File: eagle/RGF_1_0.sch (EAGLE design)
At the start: 14 parts, among them IC1 74HC670N, X1 IN, X2 Addr, X3 MODE, X4 OUT

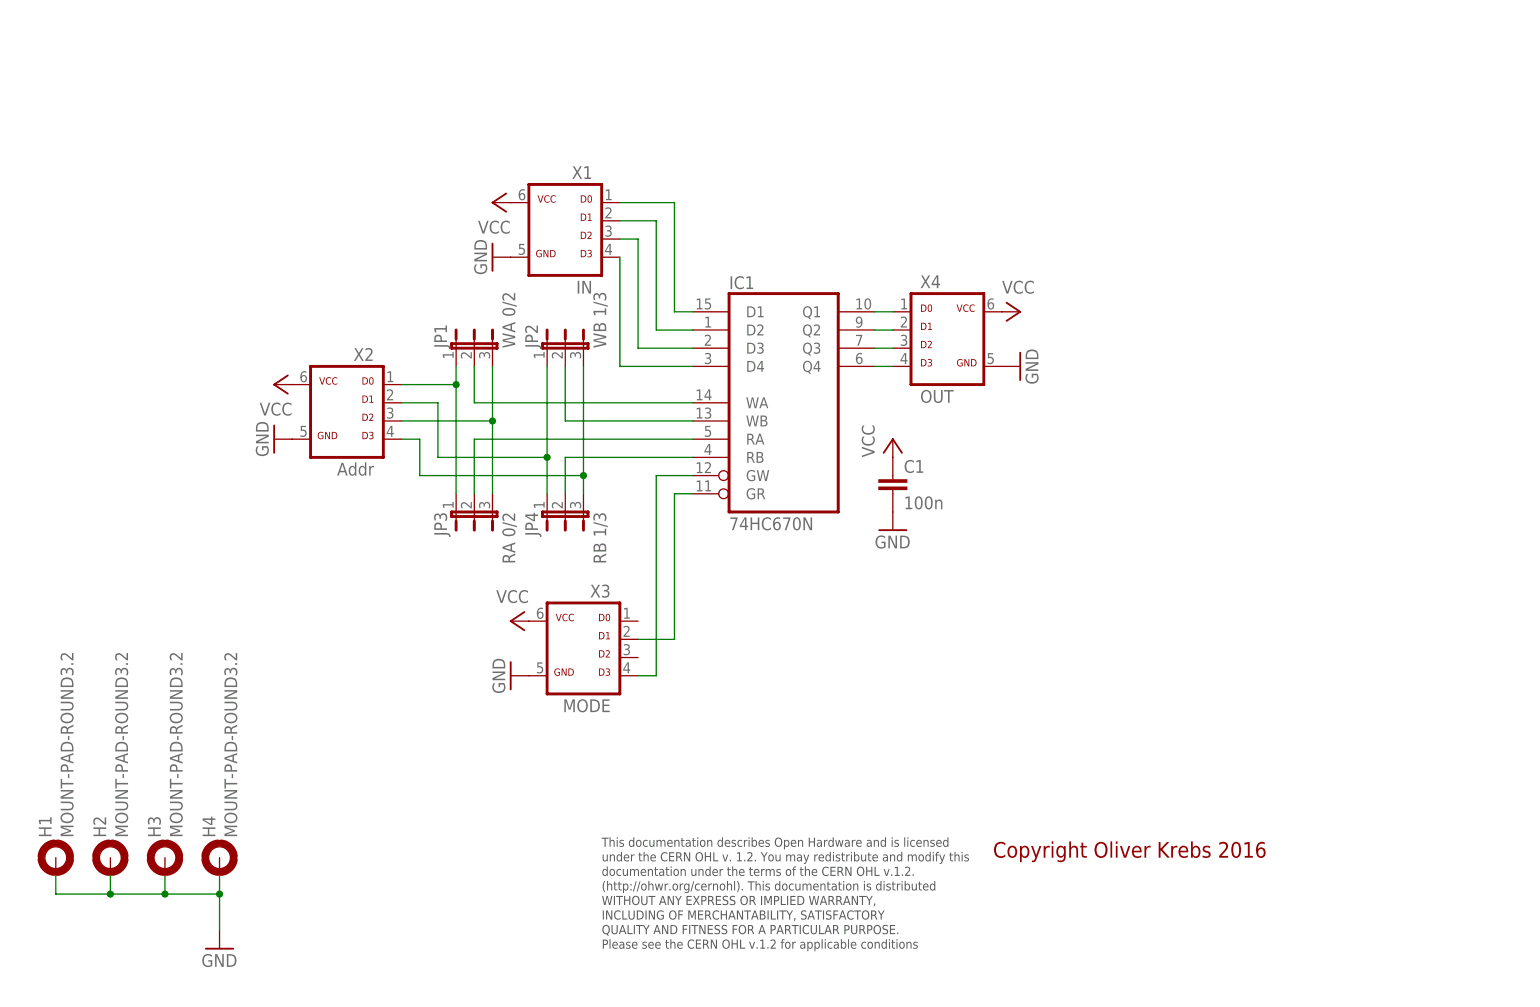
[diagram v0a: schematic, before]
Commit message: Add new tetra-Board and arduino files
Add AMP_1_0, AVC_1_0, D18_1_1, IOP_1_2, MIC_1_0, PIN_1_1, POT_1_0, PWA_1_0, PWR_1_0, RGF 2.0, SOC_2_0, VLT_1_0
Add mex_nano_shield_keyboard, mex_nano_shied_numbers

New arduino projects
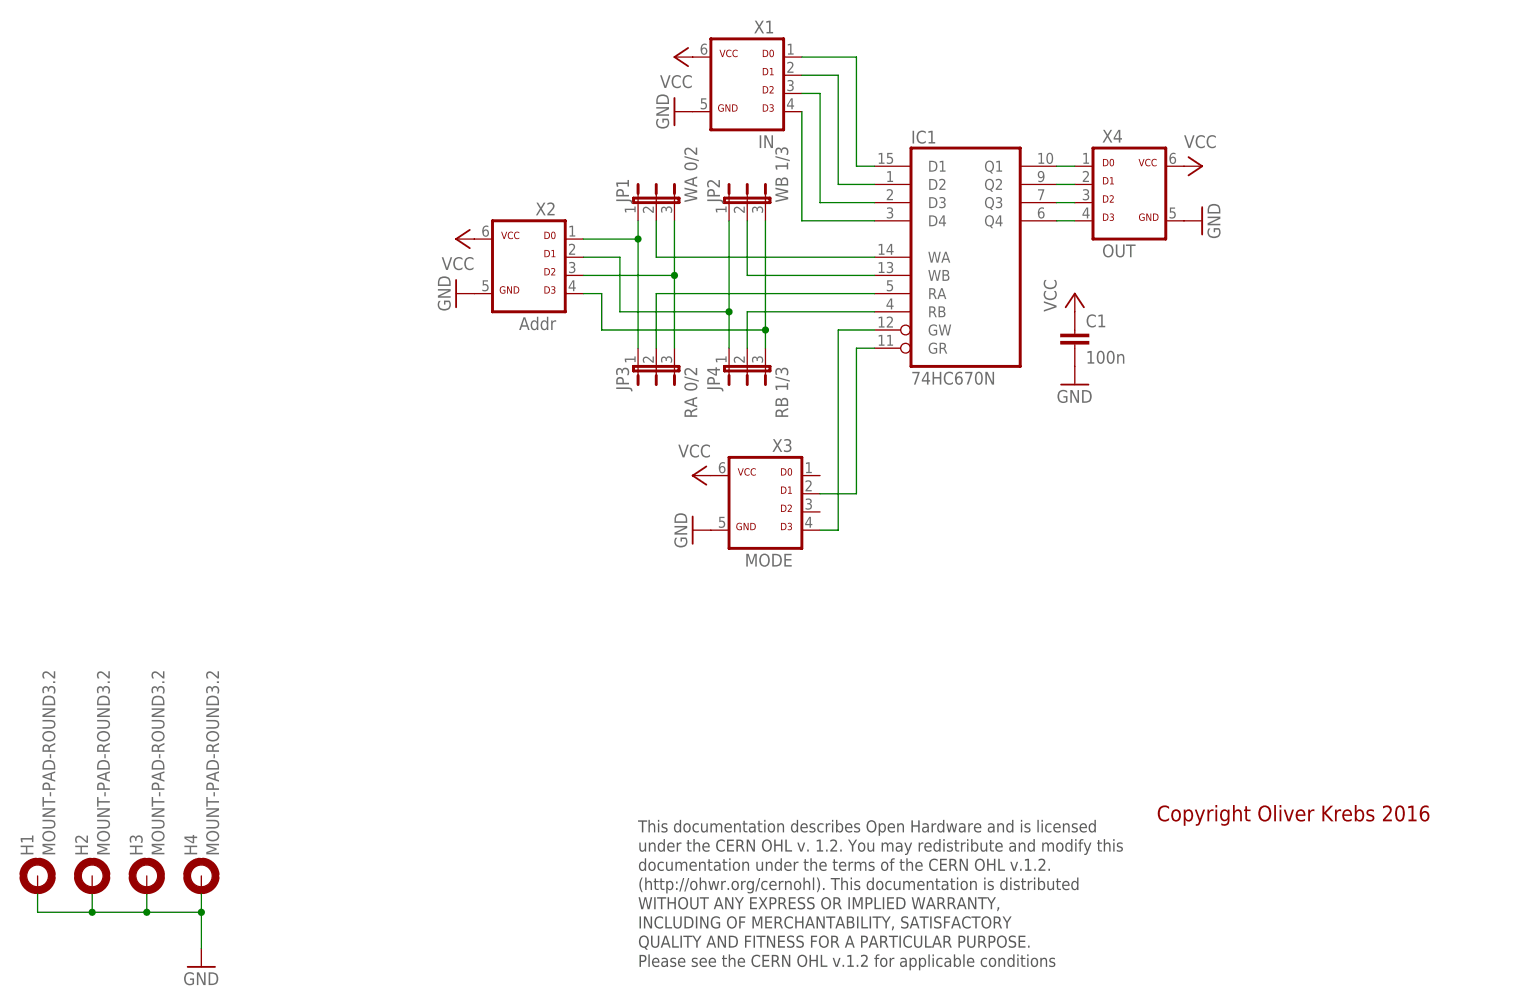
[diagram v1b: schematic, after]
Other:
- moved on the sheet: C1, H1, H2, H3, H4, IC1, JP1, JP2, JP3, JP4, X1, X2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
